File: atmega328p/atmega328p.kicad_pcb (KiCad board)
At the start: 2 copper layers, 48.3 x 48.3 mm, 27 parts, among them J1 AVR-ISP-6, J2 PB, J3 PC, J4 I2C, J5 PD, J6 I2C, J7 USB_B_Mini, SW1 SW_Clock, SW2 SW_Push, U1 ATmega328P-PU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

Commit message: atmega328p: Improved silkscreen labels
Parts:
- R3: value 15Ω -> 330Ω

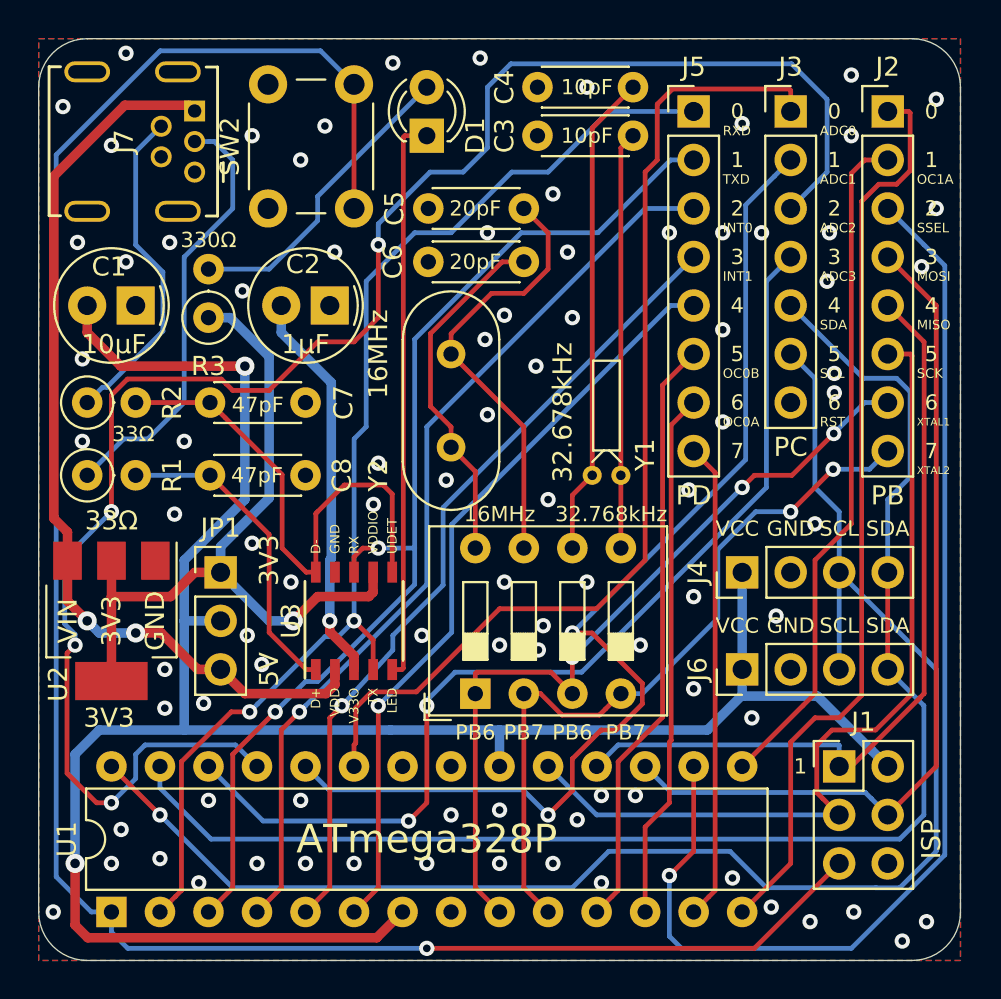
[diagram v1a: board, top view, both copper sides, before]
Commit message: treewide: Update to KiCAD 7
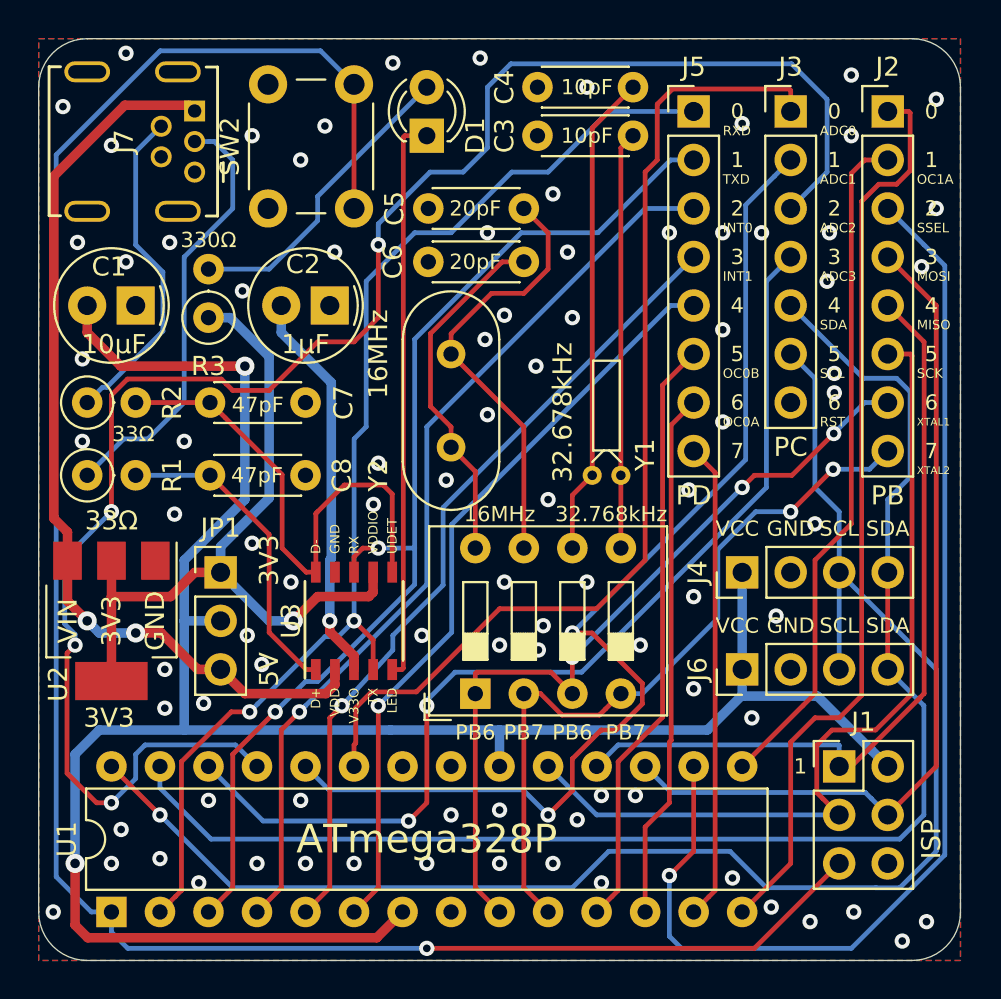
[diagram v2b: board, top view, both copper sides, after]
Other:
- net class Default removed
- net class Power removed
